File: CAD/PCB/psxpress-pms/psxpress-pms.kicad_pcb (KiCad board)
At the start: 2 copper layers, 30 parts, among them IC1 BQ25606RGER, IC2 MAX16054AZT+T, IC3 TPS61023DRLT, IC4 TPS564255DRLR

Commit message: pms - I really need to make sure to save these dang files before pushing changes.
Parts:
- moved R2 19.7 mm to (162.1, 96.1)
- moved R5 19.7 mm to (162.1, 103.6)
- moved R1 19.7 mm to (162.1, 93.6)
- moved R3 19.7 mm to (162.1, 98.6)
- moved R4 19.7 mm to (162.1, 101.1)
- moved C3 19.7 mm to (154.1, 102.1)
- moved C8 19.7 mm to (158.5, 102.1)
- moved C1 19.7 mm to (154.1, 96.0)
- moved C2 19.7 mm to (154.1, 99.1)
- moved C4 19.7 mm to (154.1, 105.1)
- moved C5 19.7 mm to (154.1, 108.1)
- moved C6 19.7 mm to (158.5, 96.0)
- moved C7 19.7 mm to (158.5, 99.1)
- moved IC1 19.7 mm to (160.7, 108.4)
- moved IC2 19.7 mm to (154.9, 116.0)
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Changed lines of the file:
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@@
   (net 29 "+3.5V")
   (footprint "Resistor_SMD:R_0603_1608Metric" (layer "F.Cu")
-    (at 142.605 98.26)
+    (at 162.145 96.085)
     (descr "Resistor SMD 0603 (1608 Metric), square (rectangular) end terminal, IPC_7351 nominal, (Body size source: IPC-SM-782 page 72, https://www.pcb-3d.com/wordpress/wp-content/uploads/ipc-sm-782a_amendment_1_and_2.pdf), generated with kicad-footprint-generator")
     (tags "resistor")
@@
   )
   (footprint "BQ25606RGER:QFN50P400X400X100-25N-D" (layer "F.Cu")
-    (at 141.16 110.6)
+    (at 160.7 108.425)
     (descr "BQ25606RGER_a")
     (tags "Integrated Circuit")
@@
   )
   (footprint "Capacitor_SMD:C_0805_2012Metric" (layer "F.Cu")
-    (at 134.52 98.2225)
+    (at 154.06 96.0475)
     (descr "Capacitor SMD 0805 (2012 Metric), square (rectangular) end terminal, IPC_7351 nominal, (Body size source: IPC-SM-782 page 76, https://www.pcb-3d.com/wordpress/wp-content/uploads/ipc-sm-782a_amendment_1_and_2.pdf, https://docs.google.com/spreadsheets/d/1BsfQQcO9C6DZCsRaXUlFlo91Tg2WpOkGARC1WS5S8t0/edit?usp=sharing), generated with kicad-footprint-generator")
     (tags "capacitor")
@@
   )
   (footprint "Resistor_SMD:R_0603_1608Metric" (layer "F.Cu")
-    (at 142.605 103.28)
+    (at 162.145 101.105)
     (descr "Resistor SMD 0603 (1608 Metric), square (rectangular) end terminal, IPC_7351 nominal, (Body size source: IPC-SM-782 page 72, https://www.pcb-3d.com/wordpress/wp-content/uploads/ipc-sm-782a_amendment_1_and_2.pdf), generated with kicad-footprint-generator")
     (tags "resistor")
@@
   )
   (footprint "Resistor_SMD:R_0603_1608Metric" (layer "F.Cu")
-    (at 142.605 100.77)
+    (at 162.145 98.595)
     (descr "Resistor SMD 0603 (1608 Metric), square (rectangular) end terminal, IPC_7351 nominal, (Body size source: IPC-SM-782 page 72, https://www.pcb-3d.com/wordpress/wp-content/uploads/ipc-sm-782a_amendment_1_and_2.pdf), generated with kicad-footprint-generator")
     (tags "resistor")
@@
   )
   (footprint "Capacitor_SMD:C_0805_2012Metric" (layer "F.Cu")
-    (at 134.52 107.2525)
+    (at 154.06 105.0775)
     (descr "Capacitor SMD 0805 (2012 Metric), square (rectangular) end terminal, IPC_7351 nominal, (Body size source: IPC-SM-782 page 76, https://www.pcb-3d.com/wordpress/wp-content/uploads/ipc-sm-782a_amendment_1_and_2.pdf, https://docs.google.com/spreadsheets/d/1BsfQQcO9C6DZCsRaXUlFlo91Tg2WpOkGARC1WS5S8t0/edit?usp=sharing), generated with kicad-footprint-generator")
     (tags "capacitor")
@@
   )
   (footprint "Resistor_SMD:R_0603_1608Metric" (layer "F.Cu")
-    (at 142.605 105.79)
+    (at 162.145 103.615)
     (descr "Resistor SMD 0603 (1608 Metric), square (rectangular) end terminal, IPC_7351 nominal, (Body size source: IPC-SM-782 page 72, https://www.pcb-3d.com/wordpress/wp-content/uploads/ipc-sm-782a_amendment_1_and_2.pdf), generated with kicad-footprint-generator")
     (tags "resistor")
@@
   )
   (footprint "MAX16054AZT+T:SOT95P275X110-6N" (layer "F.Cu")
-    (at 135.4 118.175)
+    (at 154.94 116)
     (descr "THIN SOT23")
     (tags "Integrated Circuit")
@@
   )
   (footprint "Capacitor_SMD:C_0805_2012Metric" (layer "F.Cu")
-    (at 138.97 101.2325)
+    (at 158.51 99.0575)
     (descr "Capacitor SMD 0805 (2012 Metric), square (rectangular) end terminal, IPC_7351 nominal, (Body size source: IPC-SM-782 page 76, https://www.pcb-3d.com/wordpress/wp-content/uploads/ipc-sm-782a_amendment_1_and_2.pdf, https://docs.google.com/spreadsheets/d/1BsfQQcO9C6DZCsRaXUlFlo91Tg2WpOkGARC1WS5S8t0/edit?usp=sharing), generated with kicad-footprint-generator")
     (tags "capacitor")
@@
   )
   (footprint "Capacitor_SMD:C_0805_2012Metric" (layer "F.Cu")
-    (at 138.97 98.2225)
+    (at 158.51 96.0475)
     (descr "Capacitor SMD 0805 (2012 Metric), square (rectangular) end terminal, IPC_7351 nominal, (Body size source: IPC-SM-782 page 76, https://www.pcb-3d.com/wordpress/wp-content/uploads/ipc-sm-782a_amendment_1_and_2.pdf, https://docs.google.com/spreadsheets/d/1BsfQQcO9C6DZCsRaXUlFlo91Tg2WpOkGARC1WS5S8t0/edit?usp=sharing), generated with kicad-footprint-generator")
     (tags "capacitor")
@@
   )
   (footprint "Resistor_SMD:R_0603_1608Metric" (layer "F.Cu")
-    (at 142.605 95.75)
+    (at 162.145 93.575)
     (descr "Resistor SMD 0603 (1608 Metric), square (rectangular) end terminal, IPC_7351 nominal, (Body size source: IPC-SM-782 page 72, https://www.pcb-3d.com/wordpress/wp-content/uploads/ipc-sm-782a_amendment_1_and_2.pdf), generated with kicad-footprint-generator")
     (tags "resistor")
@@
   )
   (footprint "Resistor_SMD:R_0603_1608Metric" (layer "F.Cu")
-    (at 139.215 115.955)
+    (at 158.755 113.78)
     (descr "Resistor SMD 0603 (1608 Metric), square (rectangular) end terminal, IPC_7351 nominal, (Body size source: IPC-SM-782 page 72, https://www.pcb-3d.com/wordpress/wp-content/uploads/ipc-sm-782a_amendment_1_and_2.pdf), generated with kicad-footprint-generator")
     (tags "resistor")
@@
   )
   (footprint "Capacitor_SMD:C_0805_2012Metric" (layer "F.Cu")
-    (at 134.52 104.2425)
+    (at 154.06 102.0675)
     (descr "Capacitor SMD 0805 (2012 Metric), square (rectangular) end terminal, IPC_7351 nominal, (Body size source: IPC-SM-782 page 76, https://www.pcb-3d.com/wordpress/wp-content/uploads/ipc-sm-782a_amendment_1_and_2.pdf, https://docs.google.com/spreadsheets/d/1BsfQQcO9C6DZCsRaXUlFlo91Tg2WpOkGARC1WS5S8t0/edit?usp=sharing), generated with kicad-footprint-generator")
     (tags "capacitor")
@@
   )
   (footprint "Capacitor_SMD:C_0805_2012Metric" (layer "F.Cu")
-    (at 134.52 101.2325)
+    (at 154.06 99.0575)
     (descr "Capacitor SMD 0805 (2012 Metric), square (rectangular) end terminal, IPC_7351 nominal, (Body size source: IPC-SM-782 page 76, https://www.pcb-3d.com/wordpress/wp-content/uploads/ipc-sm-782a_amendment_1_and_2.pdf, https://docs.google.com/spreadsheets/d/1BsfQQcO9C6DZCsRaXUlFlo91Tg2WpOkGARC1WS5S8t0/edit?usp=sharing), generated with kicad-footprint-generator")
     (tags "capacitor")
@@
   )
   (footprint "Capacitor_SMD:C_0805_2012Metric" (layer "F.Cu")
-    (at 134.52 110.2625)
+    (at 154.06 108.0875)
     (descr "Capacitor SMD 0805 (2012 Metric), square (rectangular) end terminal, IPC_7351 nominal, (Body size source: IPC-SM-782 page 76, https://www.pcb-3d.com/wordpress/wp-content/uploads/ipc-sm-782a_amendment_1_and_2.pdf, https://docs.google.com/spreadsheets/d/1BsfQQcO9C6DZCsRaXUlFlo91Tg2WpOkGARC1WS5S8t0/edit?usp=sharing), generated with kicad-footprint-generator")
     (tags "capacitor")
@@
   )
   (footprint "Capacitor_SMD:C_0805_2012Metric" (layer "F.Cu")
-    (at 138.97 104.2425)
+    (at 158.51 102.0675)
     (descr "Capacitor SMD 0805 (2012 Metric), square (rectangular) end terminal, IPC_7351 nominal, (Body size source: IPC-SM-782 page 76, https://www.pcb-3d.com/wordpress/wp-content/uploads/ipc-sm-782a_amendment_1_and_2.pdf, https://docs.google.com/spreadsheets/d/1BsfQQcO9C6DZCsRaXUlFlo91Tg2WpOkGARC1WS5S8t0/edit?usp=sharing), generated with kicad-footprint-generator")
     (tags "capacitor")

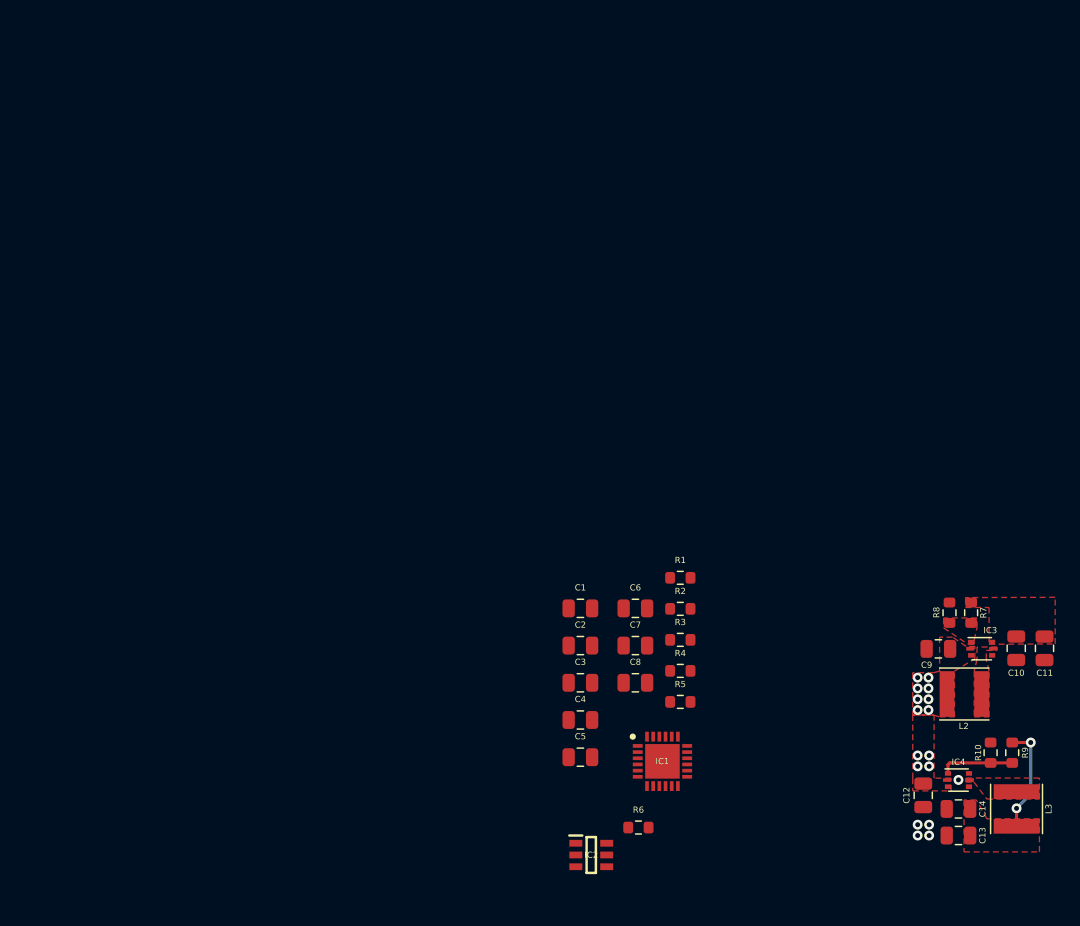
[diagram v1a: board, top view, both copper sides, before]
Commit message: pms - add voltage reg solder pads + preliminary board edge cuts
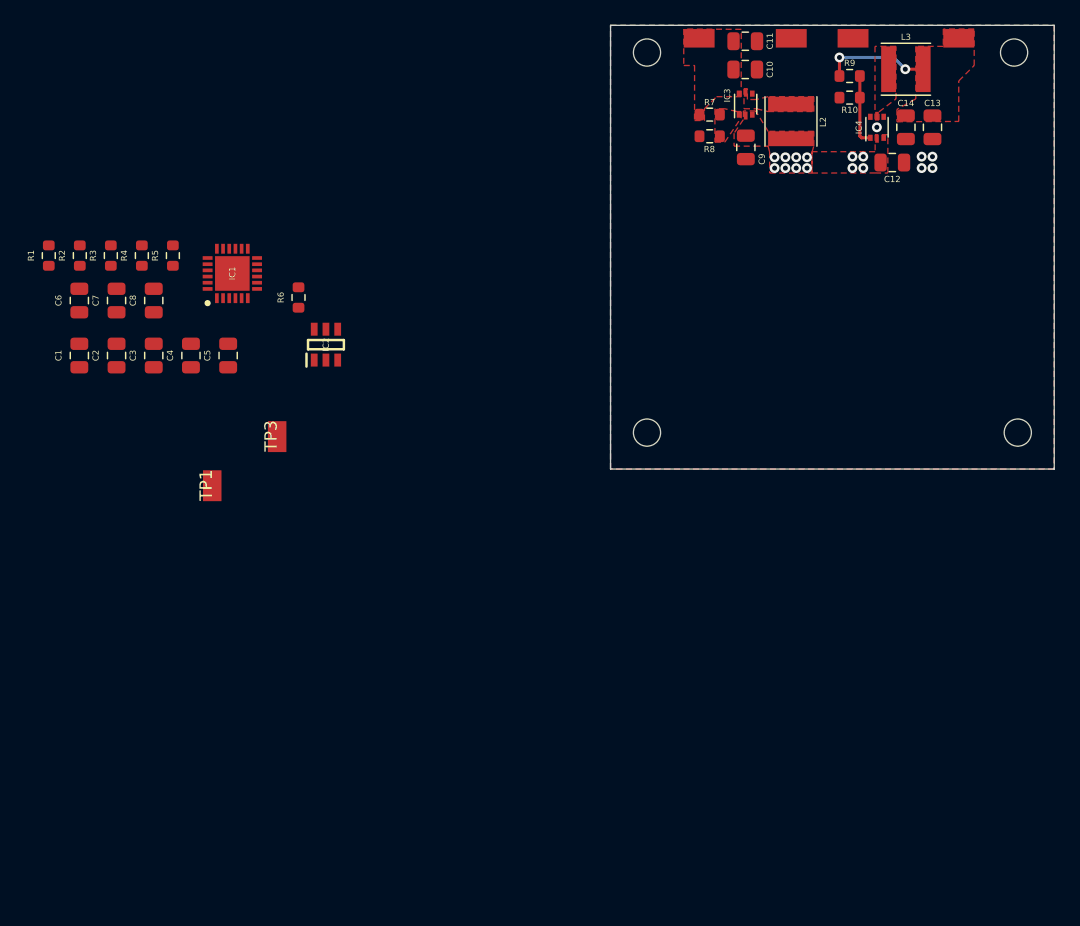
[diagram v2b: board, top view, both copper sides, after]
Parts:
- added REF**: MountingHole_2.2mm_M2, MountingHole:MountingHole_2.2mm_M2, F.Cu at (189.2, 51.1)
- added REF**: MountingHole_2.2mm_M2, MountingHole:MountingHole_2.2mm_M2, F.Cu at (159.4, 81.8)
- added REF**: MountingHole_2.2mm_M2, MountingHole:MountingHole_2.2mm_M2, F.Cu at (189.4, 81.8)
- added REF**: MountingHole_2.2mm_M2, MountingHole:MountingHole_2.2mm_M2, F.Cu at (159.4, 51.1)
- added TP1: GND, solderpads:power_pad_2.5x1.5mm, F.Cu at (124.3, 86.1)
- added TP3: BAT, solderpads:power_pad_2.5x1.5mm, F.Cu at (129.5, 82.1)
- added TP5: +5V, solderpads:power_pad_2.5x1.5mm, F.Cu at (163.7, 49.9)
- added TP6: +3V5, solderpads:power_pad_2.5x1.5mm, F.Cu at (184.7, 49.9)
- added TP7: GND, solderpads:power_pad_2.5x1.5mm, F.Cu at (171.2, 49.9)
- added TP8: GND, solderpads:power_pad_2.5x1.5mm, F.Cu at (176.2, 49.9)
- moved L3 60.5 mm to (180.4, 52.4), turned to 0 degrees
- moved R1 57.4 mm to (111.0, 67.5), turned to 90 degrees
- moved C13 57.3 mm to (182.5, 57.1), turned to -90 degrees
- moved R2 56.4 mm to (113.6, 67.5), turned to 90 degrees
- moved R9 56.3 mm to (175.8, 53.0), turned to 0 degrees
- moved R3 55.6 mm to (116.1, 67.5), turned to 90 degrees
- moved C14 55.3 mm to (180.4, 57.1), turned to -90 degrees
- moved R4 55.0 mm to (118.6, 67.5), turned to 90 degrees
- moved C11 54.8 mm to (167.4, 50.2), turned to 0 degrees
- moved R5 54.7 mm to (121.1, 67.5), turned to 90 degrees
- moved R10 54.2 mm to (175.8, 54.7), turned to 180 degrees
- moved IC4 53.2 mm to (178.1, 57.1), turned to 90 degrees
- moved IC1 52.6 mm to (125.9, 69.0), turned to 90 degrees
- moved C10 51.7 mm to (167.4, 52.5), turned to 0 degrees
- moved C6 51.4 mm to (113.5, 71.1), turned to 90 degrees
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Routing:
- added copper zone on B.Cu, net GND
- added copper zone on F.Cu, net GND
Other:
- board outline added: 35.9 x 35.9 mm

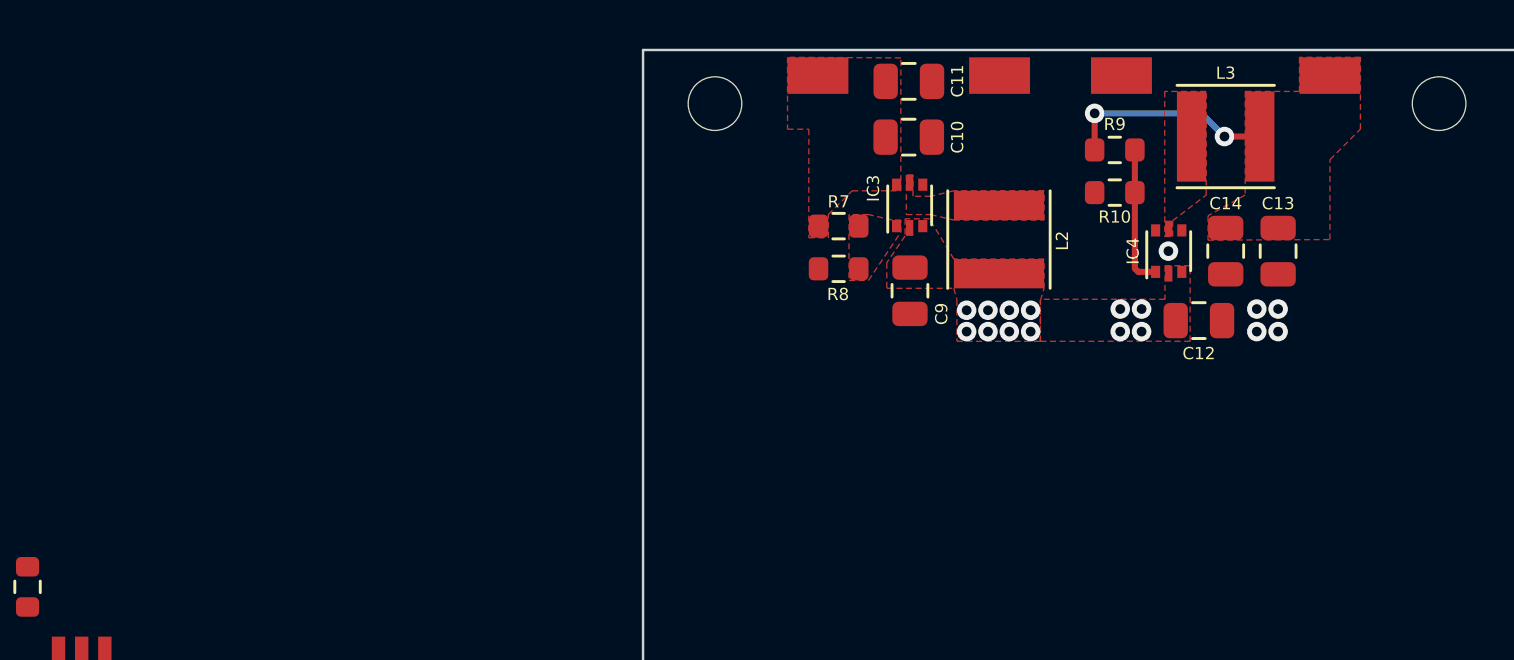
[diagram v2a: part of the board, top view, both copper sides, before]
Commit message: pms - optimize regulator layout & add 3D models for inductors
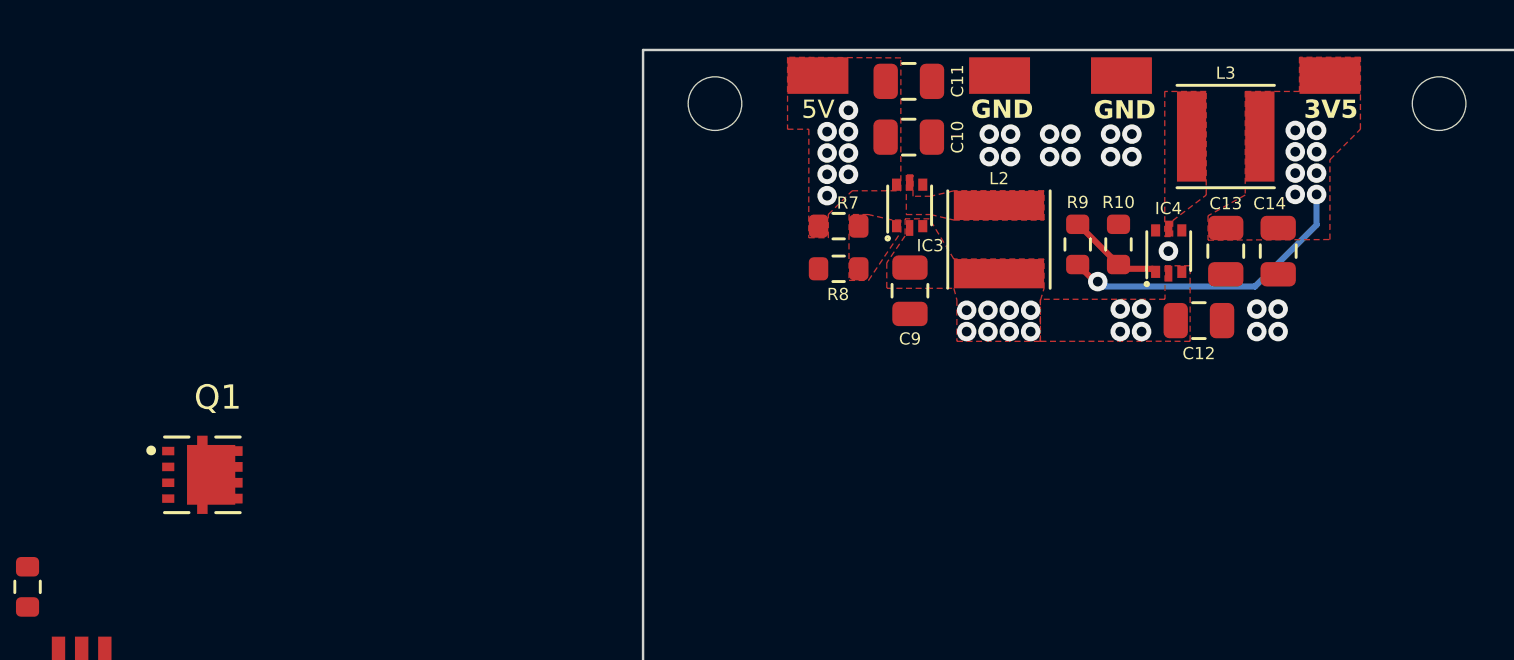
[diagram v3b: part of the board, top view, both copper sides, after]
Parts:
- added Q1: AONR21117, TRANS_AONR21321:TRANS_AONR21321, F.Cu at (138.4, 66.3)
- moved R9 4.16 mm to (174.3, 56.9), turned to 90 degrees
- moved C14 2.15 mm to (182.6, 57.1)
- moved C13 2.15 mm to (180.4, 57.1)
- moved R10 2.13 mm to (176.0, 56.9), turned to 90 degrees
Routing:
- net +3.5V: track 8.67 -> 12.5 mm, vias 2 -> 9
- net Net-(IC4-FB): track 5.97 -> 4.00 mm
- net GND: vias 5 -> 17
- net +5V: vias 0 -> 8
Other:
- board text added: "3V5"
- board text added: "5V"
- board text added: "GND"
